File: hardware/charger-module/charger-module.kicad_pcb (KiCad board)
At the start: 4 copper layers, 80 x 24.3 mm, 78 parts, among them J1 Bus_PCI_Express_x1, J2 Conn_01x06_Pin, J3 RP_USB, J4 USB_C_Receptacle_USB2.0_14P, SW1 BOOT, SW2 RESET, U1 AMS1117-3.3, U2 W25Q32JVSSIQ, U3 RP2040, U4 MPQ4242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

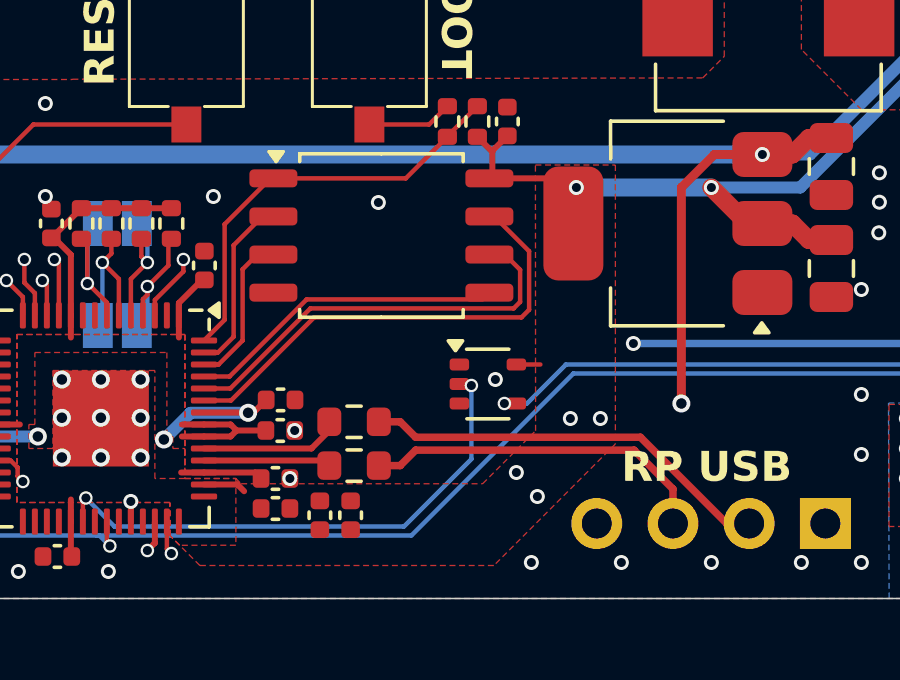
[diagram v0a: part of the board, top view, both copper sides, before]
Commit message: fix: add qr code for serial numbers
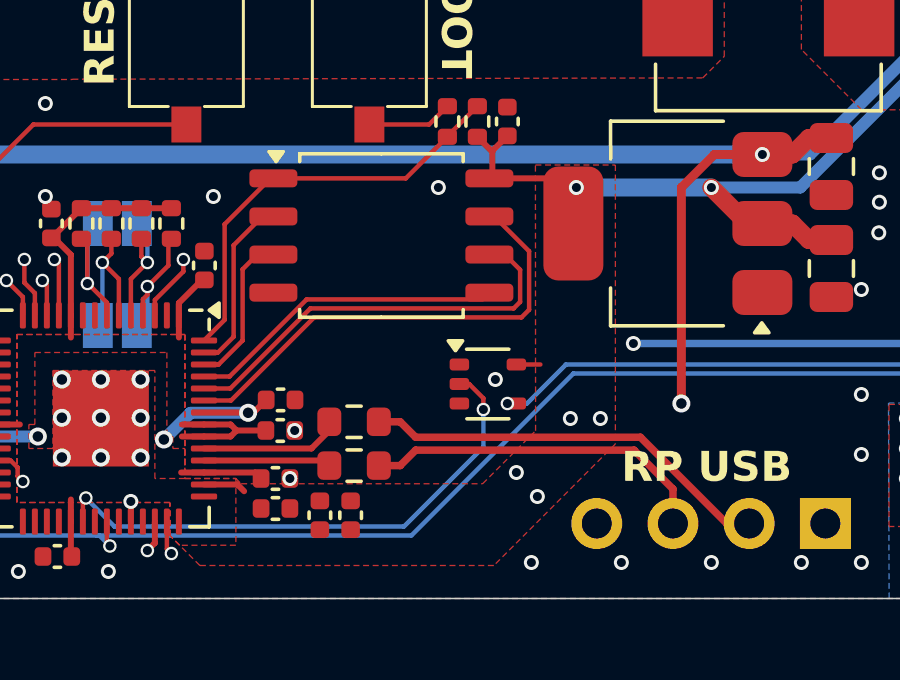
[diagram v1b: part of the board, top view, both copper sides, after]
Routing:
- net /GPIO22: track 17.5 -> 18.2 mm
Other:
- board text removed: "I2C Combine"
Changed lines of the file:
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@@
 		)
 		(fp_text user "${REFERENCE}"
-			(at 0 -3.81 360)
+			(at 0 -3.81 0)
 			(layer "B.Fab")
 			(effects
@@
 		)
 	)
+	(gr_rect
+		(start 51.6 36.3)
+		(end 56.6 41.3)
+		(stroke
+			(width 0.1)
+			(type solid)
+		)
+		(fill solid)
+		(layer "B.SilkS")
+	)
 	(gr_arc
 		(start 34 27)
@@
 		(layer "Edge.Cuts")
 	)
-	(gr_text "I2C Combine"
-		(at 49.3 39.5 270)
-		(layer "B.SilkS")
-		(effects
-			(font
-				(size 1 1)
-				(thickness 0.15)
-			)
-			(justify bottom mirror)
-		)
-	)
 	(gr_text "WARNING:\nHOT SURFACE"
 		(at 95 44 0)
@@
 			(justify bottom mirror)
 		)
-		(render_cache "Smart Module\nv0.11.7" 0
+		(render_cache "Smart Module\nv0.12.1" 0
 			(polygon
 				(pts
@@
 			(polygon
 				(pts
-					(xy 72.274964 36.296081) (xy 72.204511 36.265324) (xy 72.14747 36.238196) (xy 72.081707 36.203666)
-					(xy 72.017777 36.166022) (xy 71.95577 36.125813) (xy 71.89651 36.08359) (xy 71.837926 36.03582)
-					(xy 71.79173 35.991266) (xy 71.572278 35.991266) (xy 71.572278 37.445) (xy 71.886618 37.445) (xy 71.886618 36.38987)
-					(xy 71.949258 36.428789) (xy 72.018338 36.464488) (xy 72.028035 36.469005) (xy 72.095545 36.498277)
-					(xy 72.166165 36.525593) (xy 72.180076 36.530554)
+					(xy 71.375907 36.381078) (xy 71.38291 36.454241) (xy 71.403921 36.524668) (xy 71.40778 36.533852)
+					(xy 71.441504 36.601074) (xy 71.4836 36.666043) (xy 71.489846 36.674535) (xy 71.536539 36.732859)
+					(xy 71.58814 36.789219) (xy 71.603785 36.804961) (xy 71.658823 36.858586) (xy 71.713019 36.909827)
+					(xy 71.728349 36.92403) (xy 71.78353 36.976494) (xy 71.797225 36.989975) (xy 71.848565 37.04287)
+					(xy 71.867934 37.063981) (xy 71.916126 37.119463) (xy 71.928018 37.133956) (xy 71.960624 37.187079)
+					(xy 71.331576 37.187079) (xy 71.331576 37.445) (xy 72.306472 37.445) (xy 72.310868 37.386381) (xy 72.310868 37.335823)
+					(xy 72.306283 37.26263) (xy 72.290967 37.188687) (xy 72.278262 37.151175) (xy 72.245624 37.080009)
+					(xy 72.205413 37.013331) (xy 72.192533 36.995104) (xy 72.143776 36.933455) (xy 72.093856 36.879474)
+					(xy 72.073464 36.859549) (xy 72.01953 36.80835) (xy 71.966079 36.757151) (xy 71.941573 36.73352)
+					(xy 71.886666 36.680854) (xy 71.846685 36.642295) (xy 71.795422 36.58943) (xy 71.768649 36.558398)
+					(xy 71.726334 36.497055) (xy 71.715893 36.476699) (xy 71.697139 36.40405) (xy 71.696842 36.393534)
+					(xy 71.708434 36.318975) (xy 71.749598 36.263475) (xy 71.816948 36.232962) (xy 71.88039 36.225739)
+					(xy 71.955181 36.234224) (xy 71.987002 36.243691) (xy 72.056451 36.274328) (xy 72.077494 36.286189)
+					(xy 72.138652 36.327254) (xy 72.148202 36.334916) (xy 72.192533 36.37375) (xy 72.348604 36.166388)
+					(xy 72.287667 36.115319) (xy 72.22072 36.070189) (xy 72.155328 36.03465) (xy 72.132449 36.023872)
+					(xy 72.06158 35.996776) (xy 71.987871 35.978548) (xy 71.911322 35.969187) (xy 71.867567 35.967819)
+					(xy 71.790702 35.970681) (xy 71.71425 35.980441) (xy 71.646283 35.997128) (xy 71.576117 36.024872)
+					(xy 71.512724 36.06354) (xy 71.493143 36.07956) (xy 71.443738 36.134434) (xy 71.408178 36.199451)
+					(xy 71.404483 36.208886) (xy 71.383972 36.284674) (xy 71.376158 36.363254)
 				)
 			)
@@
 			(polygon
 				(pts
-					(xy 70.4142 37.445) (xy 70.406095 37.367262) (xy 70.3946 37.287921) (xy 70.379716 37.206977) (xy 70.363913 37.134837)
-					(xy 70.361444 37.124431) (xy 70.343114 37.051817) (xy 70.323066 36.979834) (xy 70.3013 36.908483)
-					(xy 70.277816 36.837762) (xy 70.263625 36.797634) (xy 70.237508 36.728306) (xy 70.206115 36.651221)
-					(xy 70.173074 36.576425) (xy 70.138384 36.503919) (xy 70.133932 36.495017) (xy 70.097891 36.426209)
-					(xy 70.061575 36.362301) (xy 70.020391 36.296263) (xy 69.988119 36.249187) (xy 70.623028 36.249187)
-					(xy 70.623028 35.991266) (xy 69.599773 35.991266) (xy 69.599773 36.217679) (xy 69.647763 36.274764)
-					(xy 69.694245 36.338306) (xy 69.738404 36.404976) (xy 69.748516 36.421011) (xy 69.788656 36.488033)
-					(xy 69.827743 36.559405) (xy 69.861079 36.625425) (xy 69.89361 36.694776) (xy 69.902756 36.715202)
-					(xy 69.933598 36.788184) (xy 69.962652 36.863515) (xy 69.989918 36.941195) (xy 70.015396 37.021225)
-					(xy 70.029152 37.068011) (xy 70.050607 37.150414) (xy 70.068171 37.232853) (xy 70.081842 37.315327)
-					(xy 70.091622 37.397836) (xy 70.095463 37.445)
+					(xy 70.566242 36.296081) (xy 70.495788 36.265324) (xy 70.438747 36.238196) (xy 70.372984 36.203666)
+					(xy 70.309054 36.166022) (xy 70.247047 36.125813) (xy 70.187787 36.08359) (xy 70.129203 36.03582)
+					(xy 70.083007 35.991266) (xy 69.863555 35.991266) (xy 69.863555 37.445) (xy 70.177895 37.445) (xy 70.177895 36.38987)
+					(xy 70.240535 36.428789) (xy 70.309615 36.464488) (xy 70.319312 36.469005) (xy 70.386822 36.498277)
+					(xy 70.457442 36.525593) (xy 70.471353 36.530554)
 				)
 			)
@@
 	)
 	(via
-		(at 55.9 37.1)
+		(at 57.9 36.6)
 		(size 0.5)
 		(drill 0.3)
@@
 	)
 	(segment
-		(start 60.1 43.8)
-		(end 60.5 43.8)
-		(width 0.15)
+		(start 92.2 37.685)
+		(end 91.37 37.685)
+		(width 0.3)
 		(layer "F.Cu")
 		(net 14)
 	)
 	(segment
-		(start 92.2 37.685)
-		(end 91.37 37.685)
-		(width 0.3)
+		(start 60.2 43.8)
+		(end 60.5 43.8)
+		(width 0.15)
 		(layer "F.Cu")
 		(net 14)
 	)
 	(via
-		(at 60.1 43.8)
+		(at 60.2 43.8)
 		(size 0.45)
 		(drill 0.3)
@@
 	)
 	(segment
-		(start 62.15 42.5)
-		(end 86.44 42.5)
+		(start 90.405 40.925)
+		(end 91.37 39.96)
 		(width 0.15)
 		(layer "B.Cu")
@@
 	)
 	(segment
-		(start 60.85 43.8)
-		(end 62.15 42.5)
+		(start 62.15 42.5)
+		(end 86.44 42.5)
 		(width 0.15)
 		(layer "B.Cu")
@@
 	)
 	(segment
-		(start 90.405 40.925)
-		(end 91.37 39.96)
+		(start 88.015 40.925)
+		(end 90.405 40.925)
 		(width 0.15)
 		(layer "B.Cu")
@@
 	)
 	(segment
-		(start 60.1 43.8)
+		(start 60.2 43.8)
 		(end 60.85 43.8)
 		(width 0.15)
@@
 	)
 	(segment
-		(start 86.44 42.5)
-		(end 88.015 40.925)
+		(start 91.37 39.96)
+		(end 91.37 37.685)
 		(width 0.15)
 		(layer "B.Cu")
@@
 	)
 	(segment
-		(start 88.015 40.925)
-		(end 90.405 40.925)
+		(start 60.85 43.8)
+		(end 62.15 42.5)
 		(width 0.15)
 		(layer "B.Cu")
@@
 	)
 	(segment
-		(start 91.37 39.96)
-		(end 91.37 37.685)
+		(start 86.44 42.5)
+		(end 88.015 40.925)
 		(width 0.15)
 		(layer "B.Cu")
@@
 	)
 	(segment
+		(start 59.4 44)
+		(end 59.4 43.625001)
+		(width 0.15)
+		(layer "F.Cu")
+		(net 76)
+	)
+	(segment
 		(start 46.15 46.95)
 		(end 46.05 47.05)
@@
 		(net 76)
 	)
+	(segment
+		(start 58.924999 43.15)
+		(end 58.6 43.15)
+		(width 0.15)
+		(layer "F.Cu")
+		(net 76)
+	)
+	(segment
+		(start 59.4 43.625001)
+		(end 58.924999 43.15)
+		(width 0.15)
+		(layer "F.Cu")
+		(net 76)
+	)
 	(via
 		(at 46.15 46.95)
@@
 	)
 	(via
-		(at 59 43.2)
+		(at 59.4 44)
 		(size 0.45)
 		(drill 0.3)
@@
 	)
 	(segment
-		(start 47.1 47.9)
-		(end 46.15 46.95)
+		(start 59.4 45.25)
+		(end 56.75 47.9)
 		(width 0.15)
 		(layer "B.Cu")
@@
 	)
 	(segment
-		(start 59 45.65)
-		(end 56.75 47.9)
+		(start 56.75 47.9)
+		(end 47.1 47.9)
 		(width 0.15)
 		(layer "B.Cu")
@@
 	)
 	(segment
-		(start 59 43.2)
-		(end 59 45.65)
+		(start 59.4 44)
+		(end 59.4 45.25)
 		(width 0.15)
 		(layer "B.Cu")
@@
 	)
 	(segment
-		(start 56.75 47.9)
-		(end 47.1 47.9)
+		(start 47.1 47.9)
+		(end 46.15 46.95)
 		(width 0.15)
 		(layer "B.Cu")

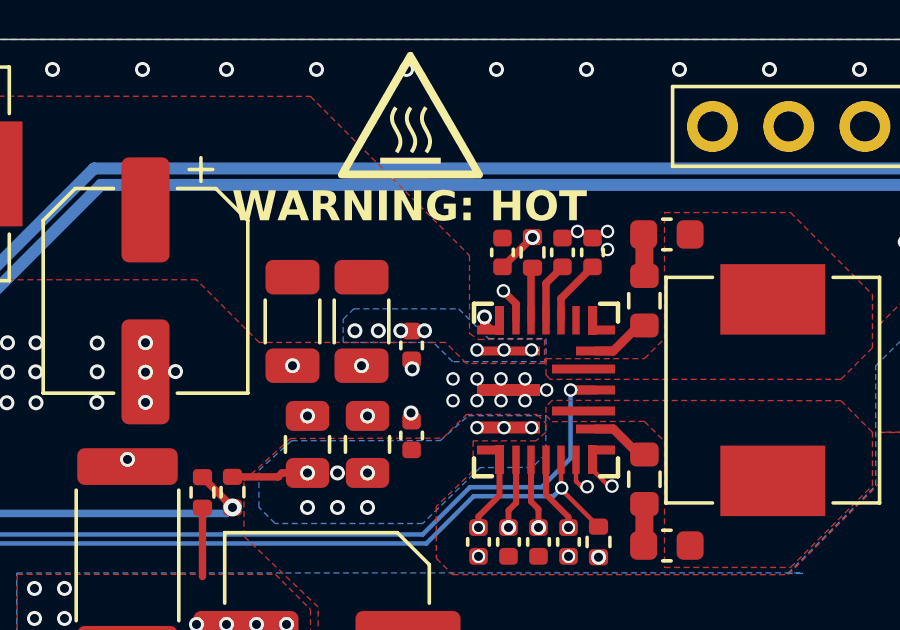
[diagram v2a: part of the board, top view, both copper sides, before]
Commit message: chore: update mpq4242 footprint
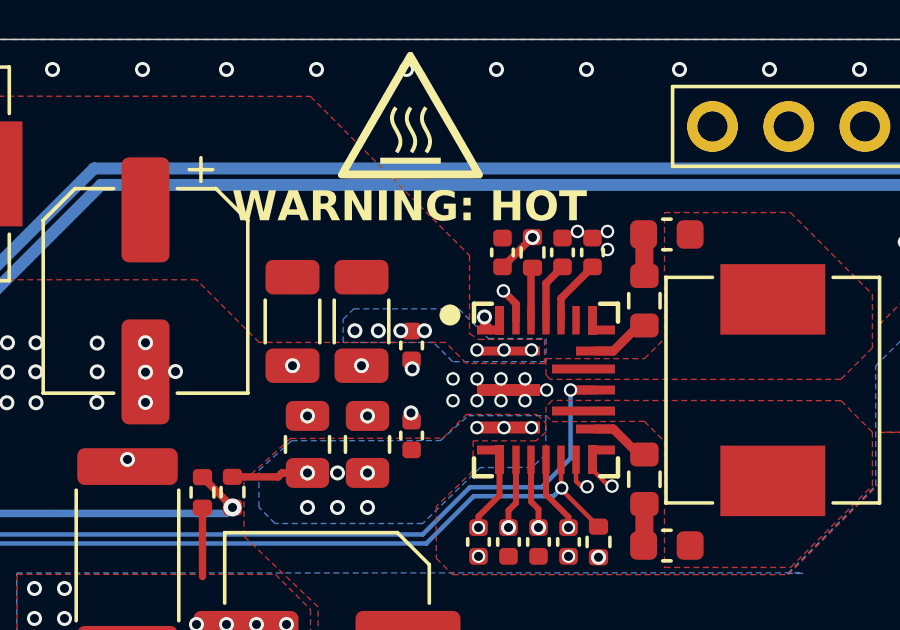
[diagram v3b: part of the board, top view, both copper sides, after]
